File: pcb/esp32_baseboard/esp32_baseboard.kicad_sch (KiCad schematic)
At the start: 91 parts, among them J1 24V IN, J14 COUNT, J15 FIBER, U1 STM32G030, U2 MP1584EN, U3 TMC1, U4 TMC2, U44 PC817, U45 PC817, U46 PC817, U47 PC817, U5 CH340C, U6 AMS1117-3.3, Y1 12MHz

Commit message: thu nhỏ board và đi dây bằng tay cho stm32
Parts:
- removed C10, C20B, C21, C3: 47u/50V, ESP32_Carrier:CP_SMD_D6.3x8, symbol ESP32_Carrier:GEN_CP_SMD_D6_3x5_8
- removed J_P24N: 24V SNS, ESP32_Carrier:JST_XH_02_Socket, symbol ESP32_Carrier:Conn_JST_XH_02
- removed J_P5N: +5V OUT, ESP32_Carrier:JST_XH_02_Socket, symbol ESP32_Carrier:Conn_JST_XH_02
- removed SW_BOOT: BOOT, ESP32_Carrier:SW_Push_6mm_SMD, symbol ESP32_Carrier:GEN_SW_Push_6mm
- removed SW_NRST: RESET, ESP32_Carrier:SW_Push_6mm_SMD, symbol ESP32_Carrier:GEN_SW_Push_6mm
- removed U2: MP1584EN, ESP32_Carrier:MP1584EN_SOIC-8-EP, symbol ESP32_Carrier:GEN_MP1584EN_SOT23_8
- added C10, C20B, C21, C3: 47u/50V, ESP32_Carrier:CP_SMD_D6.3x8, symbol ESP32_Carrier:GEN_CP_SMD_D6_3x8
- added SW_BOOT: BOOT, ESP32_Carrier:SW_Push_6mm_SMD, symbol ESP32_Carrier:GEN_SW_Push_6mm_SMD
- added SW_NRST: RESET, ESP32_Carrier:SW_Push_6mm_SMD, symbol ESP32_Carrier:GEN_SW_Push_6mm_SMD
- added U2: MP1584EN, ESP32_Carrier:MP1584EN_SOIC-8-EP, symbol ESP32_Carrier:GEN_MP1584EN_SOIC_8_EP
- C20: value 470u/50V -> 220u/50V
- D4: value SS34 -> SS54
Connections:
- net +24V: now also C21.1, U2.7
- net +24V_MOT2: now also C20B.1
- net +24V_SNS: now also J14.4 (ENC_B), C10.1
- net +3V3: now also C3.1, SW_BOOT.3, SW_BOOT.4
- net /BUCK_BS: now also U2.8
- net /BUCK_COMP: now also U2.3
- net /BUCK_FB: now also U2.4
- net /BUCK_FREQ: now also U2.6
- net /BUCK_SW: now also U2.1
- net /BUP: now also U1.11; no longer U1.14 (P14)
- net /CNT5: now also U1.14; no longer U1.39 (P39)
- net /DIR: now also U1.16; no longer U1.12 (P12)
- net /DIR2: now also U1.19; no longer U1.18 (P18)
- net /EN_TMC: now also U1.17; no longer U1.13 (P13)
- net /EN_TMC2: now also U1.20; no longer U1.28 (P28)
- net /IN2: now also U1.12; no longer U1.27 (P27)
- net /IN3: now also U1.13; no longer U1.43 (P43)
- net /KEY_C0: now also U1.44; no longer U1.23 (P23)
- net /KEY_C1: now also U1.43; no longer U1.24 (P24)
- net /KEY_C2: now also U1.42; no longer U1.25 (P25)
- net /KEY_C3: now also U1.41; no longer U1.26 (P26)
- net /KEY_R0: now also U1.48; no longer U1.19 (P19)
- net /KEY_R1: now also U1.47; no longer U1.20 (P20)
- net /KEY_R2: now also U1.46; no longer U1.21 (P21)
- net /KEY_R3: now also U1.45; no longer U1.22 (P22)
- net /NRST: now also SW_NRST.1, SW_NRST.2
- net /PWM_OUT1: now also U1.22; no longer U1.33 (P33)
- net /PWM_OUT2: now also U1.23; no longer U1.34 (P34)
- net /PWR_EN1: now also U1.24; no longer U1.44 (P44)
- net /PWR_EN2: now also U1.25; no longer U1.45 (P45)
- net /PWR_FAULT: now also U1.26; no longer U1.46 (P46)
- net /STEP: now also U1.15; no longer U1.11 (P11)
- net /STEP2: now also U1.18; no longer U1.17 (P17)
- net /SWCLK: now also SW_BOOT.1, SW_BOOT.2
- net /TM_CLK: now also U1.37; no longer U1.15 (P15)
- net /TM_DIO: now also U1.38; no longer U1.16 (P16)
- net /VIB_CTRL: now also U1.27; no longer U1.47 (P47)
- net /VIB_FAULT: now also U1.28; no longer U1.48 (P48)
- net GND: now also C10.2, C20B.2, C21.2, C3.2, SW_NRST.3, SW_NRST.4, U2.5, U2.9
- no-connect marks 32 -> 31
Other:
- note removed: "24V IN / SNS"
- note removed: "3V3"
- note removed: "BUCK +5V"
- note removed: "DO / VIB"
- note removed: "HMI"
- note removed: "MCU STM32G030"
- note removed: "OPTO IN"
- note removed: "TMC1"
- note removed: "TMC2"
- note removed: "USB-UART"

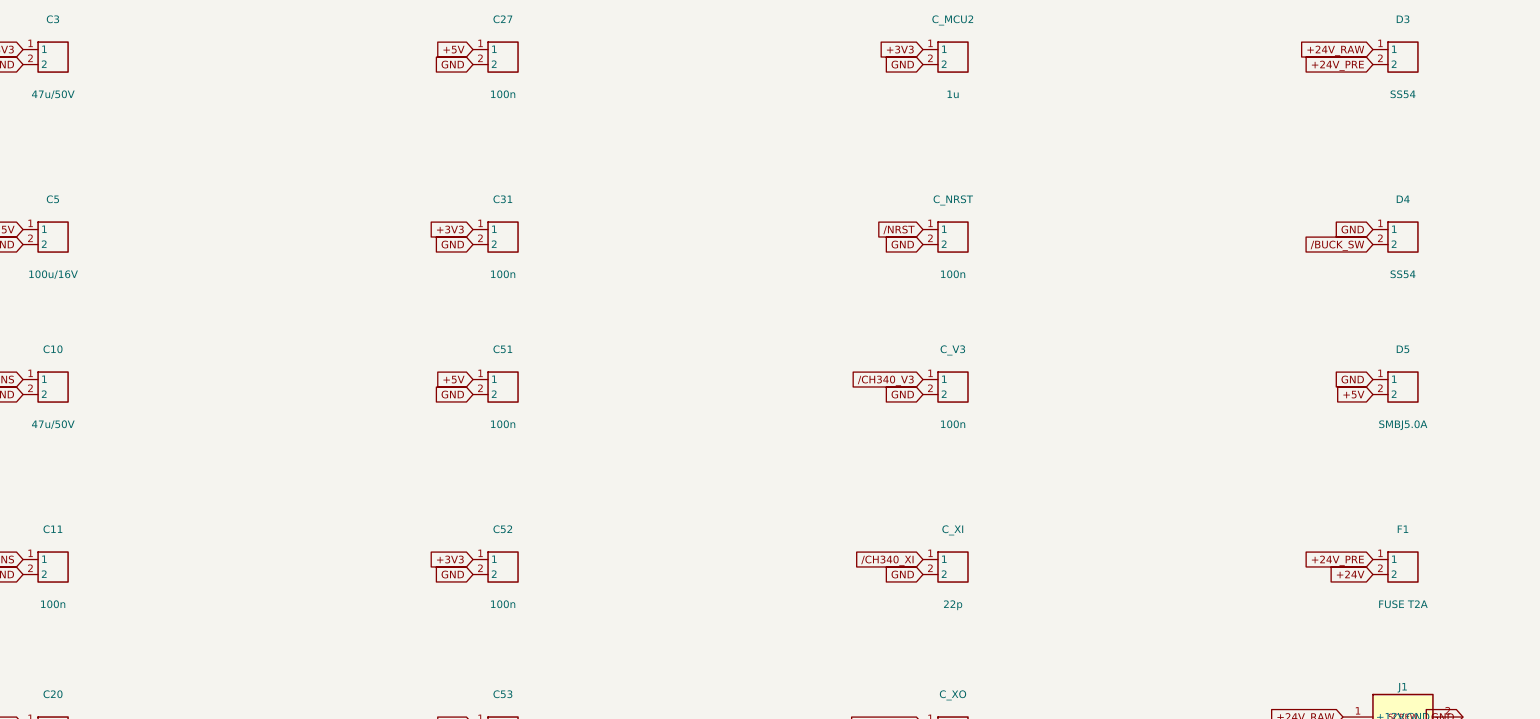
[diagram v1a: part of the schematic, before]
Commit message: đi dây bằng tay hoàn thiện cho board. không dùng LLM AI
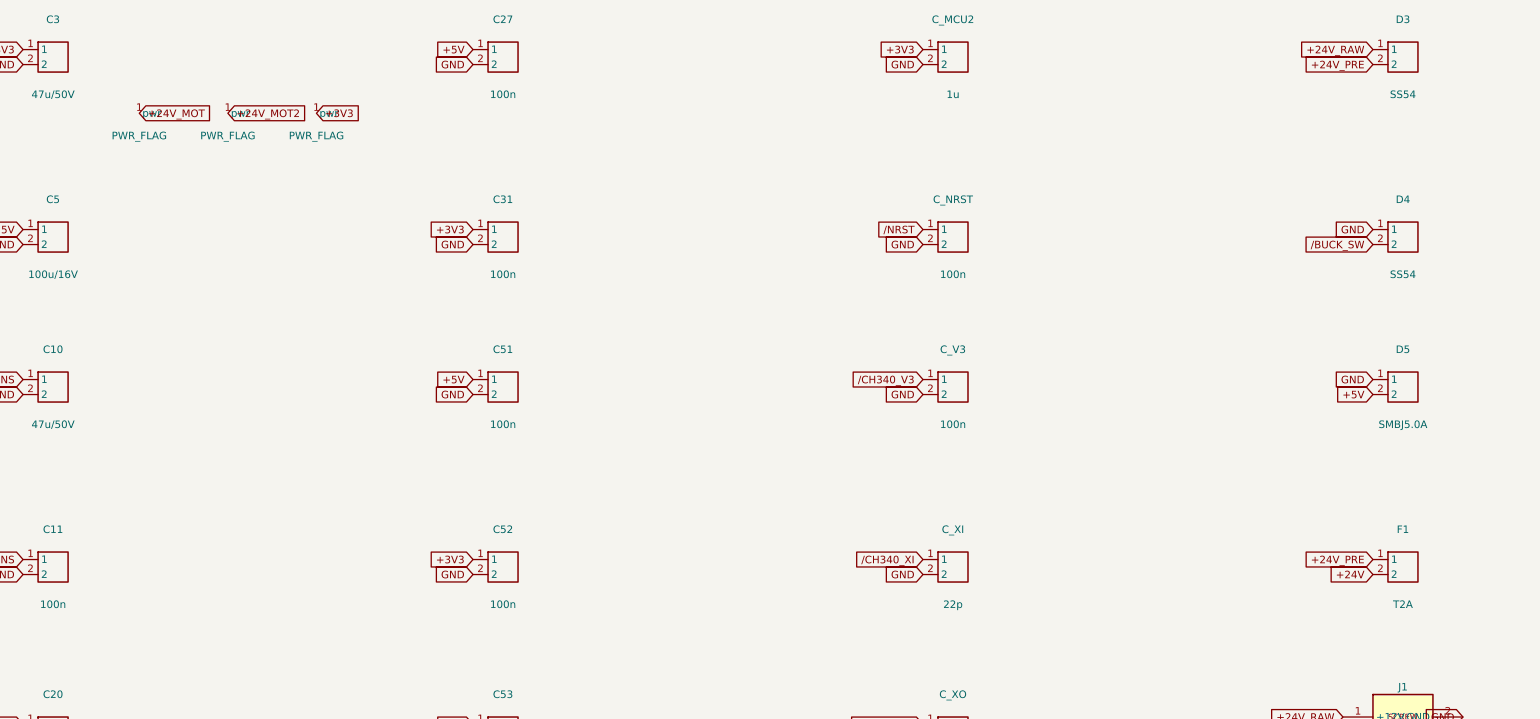
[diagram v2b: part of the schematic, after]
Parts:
- F1: value FUSE T2A -> T2A
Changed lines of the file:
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@@
 		(property "Reference" "F1" (at 254.0 110.49000000000001 0)
 			(effects (font (size 1.27 1.27))))
-		(property "Value" "FUSE T2A" (at 254.0 123.19 0)
+		(property "Value" "T2A" (at 254.0 123.19 0)
 			(effects (font (size 1.27 1.27))))
 		(property "Footprint" "ESP32_Carrier:Fuse_Holder_5x20_Open" (at 254.0 116.84 0)
@@
 		(effects (font (size 1.27 1.27)) (justify right))
 	)
+	(symbol (lib_id "ESP32_Carrier:PWR_FLAG") (at 40.0 40.0 0) (unit 1)
+		(exclude_from_sim no) (in_bom no) (on_board no) (dnp no)
+		(property "Reference" "#FLG_MOT" (at 40.0 45.08 0)
+			(effects (font (size 1.27 1.27)) (hide yes)))
+		(property "Value" "PWR_FLAG" (at 40.0 43.81 0)
+			(effects (font (size 1.27 1.27))))
+		(property "Footprint" "" (at 40.0 40.0 0)
+			(effects (font (size 1.27 1.27)) (hide yes)))
+		(property "Datasheet" "" (at 40.0 40.0 0)
+			(effects (font (size 1.27 1.27)) (hide yes)))
+		(pin "1")
+		(instances
+			(project "esp32_baseboard"
+				(path "/3cbaf1f0-c85a-4e9f-abaa-9b70a700ba67"
+					(reference "#FLG_MOT") (unit 1)
+				)
+			)
+		)
+	)
+	(global_label "+24V_MOT"
+		(shape input)
+		(at 40.0 40.0 0)
+		(effects (font (size 1.27 1.27)) (justify left))
+	)
+	(symbol (lib_id "ESP32_Carrier:PWR_FLAG") (at 55.0 40.0 0) (unit 1)
+		(exclude_from_sim no) (in_bom no) (on_board no) (dnp no)
+		(property "Reference" "#FLG_MOT2" (at 55.0 45.08 0)
+			(effects (font (size 1.27 1.27)) (hide yes)))
+		(property "Value" "PWR_FLAG" (at 55.0 43.81 0)
+			(effects (font (size 1.27 1.27))))
+		(property "Footprint" "" (at 55.0 40.0 0)
+			(effects (font (size 1.27 1.27)) (hide yes)))
+		(property "Datasheet" "" (at 55.0 40.0 0)
+			(effects (font (size 1.27 1.27)) (hide yes)))
+		(pin "1")
+		(instances
+			(project "esp32_baseboard"
+				(path "/3cbaf1f0-c85a-4e9f-abaa-9b70a700ba67"
+					(reference "#FLG_MOT2") (unit 1)
+				)
+			)
+		)
+	)
+	(global_label "+24V_MOT2"
+		(shape input)
+		(at 55.0 40.0 0)
+		(effects (font (size 1.27 1.27)) (justify left))
+	)
+	(symbol (lib_id "ESP32_Carrier:PWR_FLAG") (at 70.0 40.0 0) (unit 1)
+		(exclude_from_sim no) (in_bom no) (on_board no) (dnp no)
+		(property "Reference" "#FLG_3V3" (at 70.0 45.08 0)
+			(effects (font (size 1.27 1.27)) (hide yes)))
+		(property "Value" "PWR_FLAG" (at 70.0 43.81 0)
+			(effects (font (size 1.27 1.27))))
+		(property "Footprint" "" (at 70.0 40.0 0)
+			(effects (font (size 1.27 1.27)) (hide yes)))
+		(property "Datasheet" "" (at 70.0 40.0 0)
+			(effects (font (size 1.27 1.27)) (hide yes)))
+		(pin "1")
+		(instances
+			(project "esp32_baseboard"
+				(path "/3cbaf1f0-c85a-4e9f-abaa-9b70a700ba67"
+					(reference "#FLG_3V3") (unit 1)
+				)
+			)
+		)
+	)
+	(global_label "+3V3"
+		(shape input)
+		(at 70.0 40.0 0)
+		(effects (font (size 1.27 1.27)) (justify left))
+	)
 	(sheet_instances
